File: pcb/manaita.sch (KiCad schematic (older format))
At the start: 105 parts, among them J1 USB_B_Mini, J4 SCK, J6 MOSI, J7 MISO, J8 VCC, J9 GND, SW1 SW_PUSH, SW10 SW_PUSH, SW11 SW_PUSH, SW12 SW_PUSH, SW13 SW_PUSH, SW14 SW_PUSH, SW15 SW_PUSH, SW16 SW_PUSH, SW17 SW_PUSH, SW18 SW_PUSH, SW19 SW_PUSH, SW2 SW_PUSH, SW20 SW_PUSH, SW21 SW_PUSH, SW22 SW_PUSH, SW23 SW_PUSH, SW24 SW_PUSH, SW25 SW_PUSH, SW26 SW_PUSH, SW27 SW_PUSH, SW28 SW_PUSH, SW29 SW_PUSH, SW3 SW_PUSH, SW30 SW_PUSH, SW31 SW_PUSH, SW32 SW_PUSH, SW33 SW_PUSH, SW34 SW_PUSH, SW35 SW_PUSH, SW36 SW_PUSH, SW37 SW_PUSH, SW38 SW_PUSH, SW39 SW_PUSH, SW4 SW_PUSH, SW40 SW_PUSH, SW41 SW_Push, SW5 SW_PUSH, SW6 SW_PUSH, SW7 SW_PUSH, SW8 SW_PUSH, SW9 SW_PUSH, U1 ATmega32U4-AU, Y1 Crystal_GND24_Small

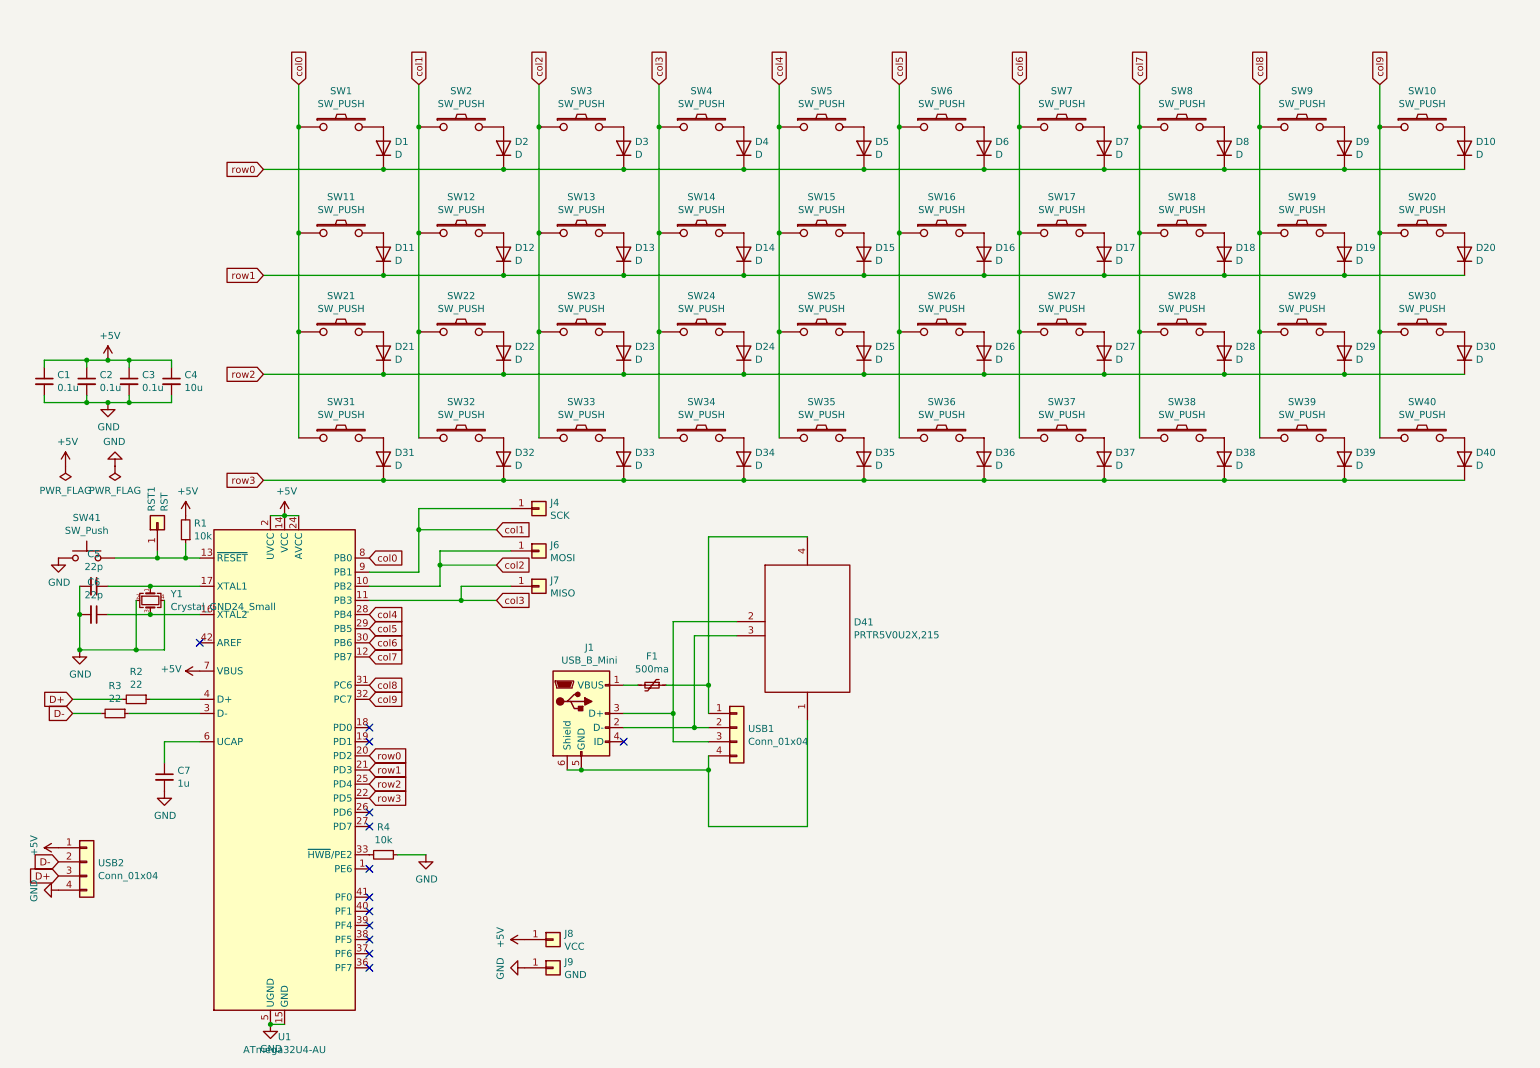
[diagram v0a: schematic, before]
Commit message: :bug: (sch) fix switch
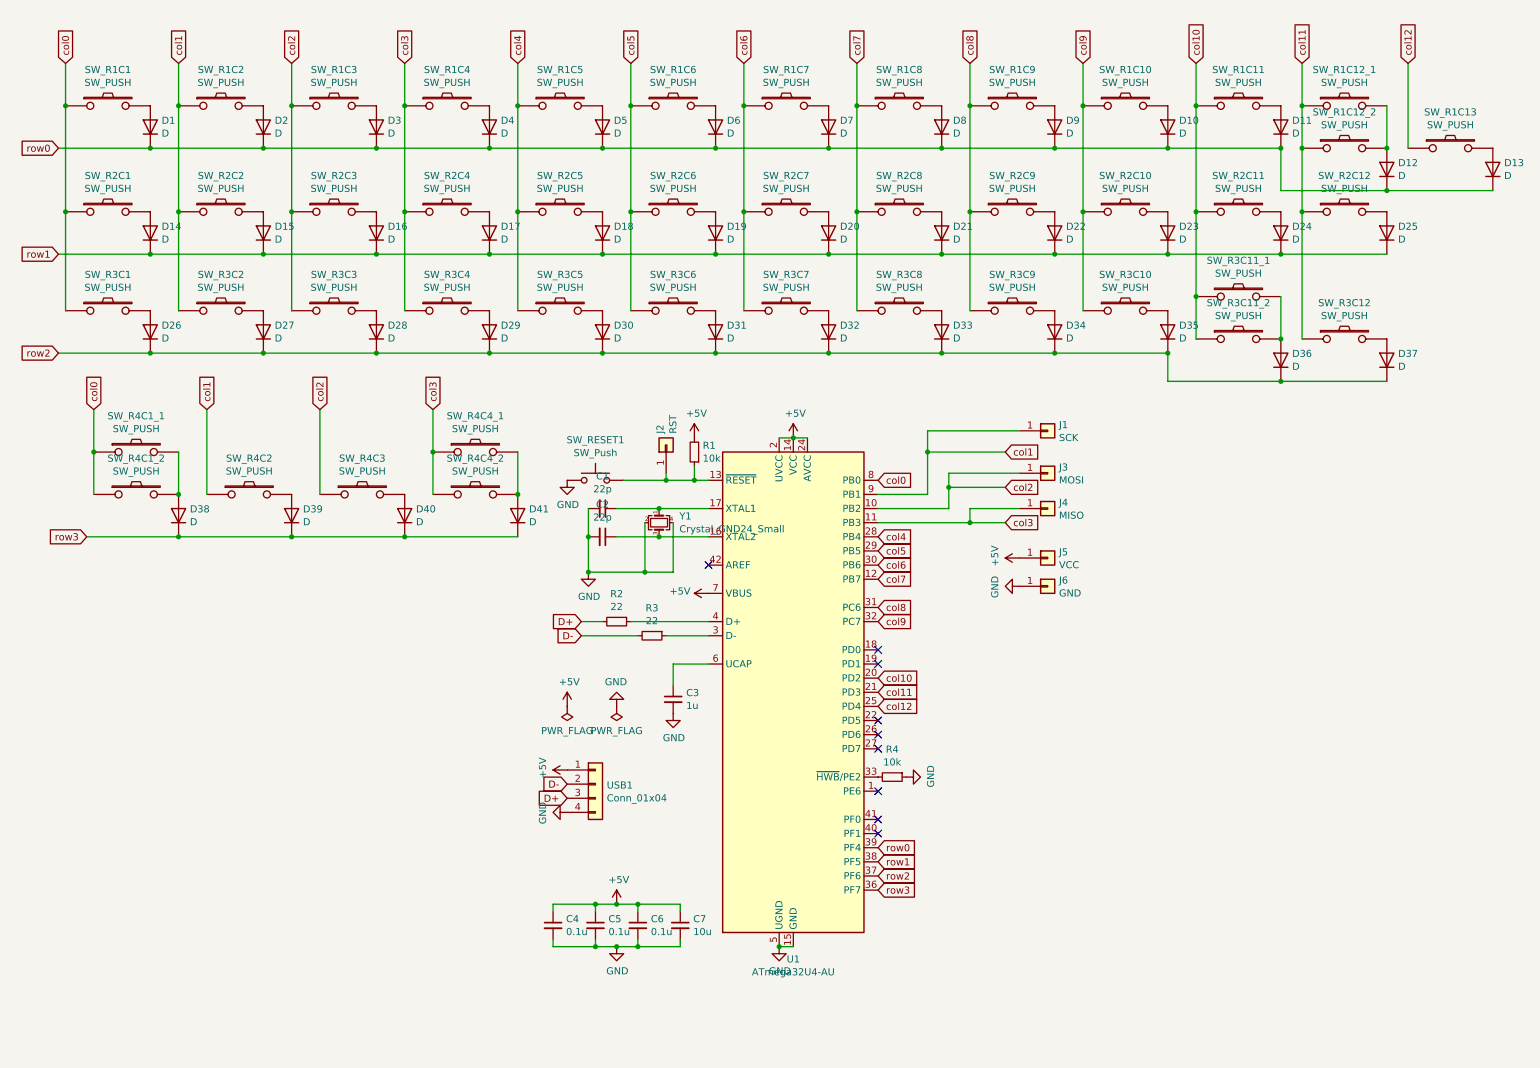
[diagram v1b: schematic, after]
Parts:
- removed D35, D38, D39, D40: D, swanmatch:D3_TH_SMD, symbol Device:D
- removed D41: PRTR5V0U2X,215, digikey:TO-253-4, symbol swanmatch:PRTR5V0U2X,215
- removed F1: 500ma, Fuse:Fuse_1206_3216Metric_Pad1.42x1.75mm_HandSolder, symbol Device:Polyfuse_Small
- removed J1: USB_B_Mini, Connector_USB:USB_Micro-B_Molex-105017-0001, symbol Connector:USB_B_Micro
- removed SW35: SW_PUSH, swanmatch:MX_Hotswap_1u, symbol swanmatch:SW_PUSH
- removed SW36, SW38, SW39: SW_PUSH, swanmatch:MX_Hotswap_1.25u, symbol swanmatch:SW_PUSH
- removed SW37: SW_PUSH, swanmatch:MX_Hotswap_2.25u, symbol swanmatch:SW_PUSH
- removed SW40: SW_PUSH, swanmatch:MX_Hotswap_2.75u, symbol swanmatch:SW_PUSH
- removed USB1: Conn_01x04, Connector_PinHeader_2.54mm:PinHeader_1x04_P2.54mm_Horizontal, symbol Connector_Generic:Conn_01x04
- added D11, D12, D13, D24, D25: D, swanmatch:D3_SMD_v2, symbol Device:D
- added SW_R1C11, SW_R1C12_1, SW_R1C12_2, SW_R1C13, SW_R2C11, SW_R3C11_1: SW_PUSH, mikamo3:CherryMX_Hotswap_1.00u_1side, symbol swanmatch:SW_PUSH
- added SW_R2C12: SW_PUSH, mikamo3:CherryMX_Hotswap_1.75u_1side, symbol swanmatch:SW_PUSH
- added SW_R3C11_2: SW_PUSH, mikamo3:CherryMX_Hotswap_2.25u_1side, symbol swanmatch:SW_PUSH
- added SW_R3C12, SW_R4C1_1, SW_R4C4_1: SW_PUSH, mikamo3:CherryMX_Hotswap_1.25u_1side, symbol swanmatch:SW_PUSH
- D1, D10, D2, D3, D36, D37, D4, D5, D6, D7, D8, D9: footprint swanmatch:D3_TH_SMD -> swanmatch:D3_SMD_v2
- D14: renamed from D11; footprint swanmatch:D3_TH_SMD -> swanmatch:D3_SMD_v2
- D15: renamed from D12; footprint swanmatch:D3_TH_SMD -> swanmatch:D3_SMD_v2
- D16: renamed from D13; footprint swanmatch:D3_TH_SMD -> swanmatch:D3_SMD_v2
- D17: renamed from D14; footprint swanmatch:D3_TH_SMD -> swanmatch:D3_SMD_v2
- D18: renamed from D15; footprint swanmatch:D3_TH_SMD -> swanmatch:D3_SMD_v2
- D19: renamed from D16; footprint swanmatch:D3_TH_SMD -> swanmatch:D3_SMD_v2
- D20: renamed from D17; footprint swanmatch:D3_TH_SMD -> swanmatch:D3_SMD_v2
- D21: renamed from D18; footprint swanmatch:D3_TH_SMD -> swanmatch:D3_SMD_v2
- D22: renamed from D19; footprint swanmatch:D3_TH_SMD -> swanmatch:D3_SMD_v2
- D23: renamed from D20; footprint swanmatch:D3_TH_SMD -> swanmatch:D3_SMD_v2
- D26: renamed from D21; footprint swanmatch:D3_TH_SMD -> swanmatch:D3_SMD_v2
- D27: renamed from D22; footprint swanmatch:D3_TH_SMD -> swanmatch:D3_SMD_v2
- D28: renamed from D23; footprint swanmatch:D3_TH_SMD -> swanmatch:D3_SMD_v2
- D29: renamed from D24; footprint swanmatch:D3_TH_SMD -> swanmatch:D3_SMD_v2
- D30: renamed from D25; footprint swanmatch:D3_TH_SMD -> swanmatch:D3_SMD_v2
- D31: renamed from D26; footprint swanmatch:D3_TH_SMD -> swanmatch:D3_SMD_v2
- D32: renamed from D27; footprint swanmatch:D3_TH_SMD -> swanmatch:D3_SMD_v2
- D33: renamed from D28; footprint swanmatch:D3_TH_SMD -> swanmatch:D3_SMD_v2
- D34: renamed from D29; footprint swanmatch:D3_TH_SMD -> swanmatch:D3_SMD_v2
- D35: renamed from D30; footprint swanmatch:D3_TH_SMD -> swanmatch:D3_SMD_v2
- D38: renamed from D31; footprint swanmatch:D3_TH_SMD -> swanmatch:D3_SMD_v2
- D39: renamed from D32; footprint swanmatch:D3_TH_SMD -> swanmatch:D3_SMD_v2
- D40: renamed from D33; footprint swanmatch:D3_TH_SMD -> swanmatch:D3_SMD_v2
- D41: renamed from D34; footprint swanmatch:D3_TH_SMD -> swanmatch:D3_SMD_v2
- SW_R1C1: renamed from SW1; footprint swanmatch:MX_Hotswap_1u -> mikamo3:CherryMX_Hotswap_1.00u_1side
- SW_R1C10: renamed from SW10; footprint swanmatch:MX_Hotswap_1u -> mikamo3:CherryMX_Hotswap_1.00u_1side
- SW_R1C2: renamed from SW2; footprint swanmatch:MX_Hotswap_1u -> mikamo3:CherryMX_Hotswap_1.00u_1side
- SW_R1C3: renamed from SW3; footprint swanmatch:MX_Hotswap_1u -> mikamo3:CherryMX_Hotswap_1.00u_1side
- SW_R1C4: renamed from SW4; footprint swanmatch:MX_Hotswap_1u -> mikamo3:CherryMX_Hotswap_1.00u_1side
- SW_R1C5: renamed from SW5; footprint swanmatch:MX_Hotswap_1u -> mikamo3:CherryMX_Hotswap_1.00u_1side
- SW_R1C6: renamed from SW6; footprint swanmatch:MX_Hotswap_1u -> mikamo3:CherryMX_Hotswap_1.00u_1side
- SW_R1C7: renamed from SW7; footprint swanmatch:MX_Hotswap_1u -> mikamo3:CherryMX_Hotswap_1.00u_1side
- SW_R1C8: renamed from SW8; footprint swanmatch:MX_Hotswap_1u -> mikamo3:CherryMX_Hotswap_1.00u_1side
- SW_R1C9: renamed from SW9; footprint swanmatch:MX_Hotswap_1u -> mikamo3:CherryMX_Hotswap_1.00u_1side
- SW_R2C1: renamed from SW11; footprint swanmatch:MX_Hotswap_1u -> mikamo3:CherryMX_Hotswap_1.25u_1side
- SW_R2C10: renamed from SW20; footprint swanmatch:MX_Hotswap_1u -> mikamo3:CherryMX_Hotswap_1.00u_1side
- SW_R2C2: renamed from SW12; footprint swanmatch:MX_Hotswap_2u -> mikamo3:CherryMX_Hotswap_1.00u_1side
- SW_R2C3: renamed from SW13; footprint swanmatch:MX_Hotswap_1.25u -> mikamo3:CherryMX_Hotswap_1.00u_1side
- SW_R2C4: renamed from SW14; footprint swanmatch:MX_Hotswap_1u -> mikamo3:CherryMX_Hotswap_1.00u_1side
- SW_R2C5: renamed from SW15; footprint swanmatch:MX_Hotswap_1u -> mikamo3:CherryMX_Hotswap_1.00u_1side
- SW_R2C6: renamed from SW16; footprint swanmatch:MX_Hotswap_1u -> mikamo3:CherryMX_Hotswap_1.00u_1side
- SW_R2C7: renamed from SW17; footprint swanmatch:MX_Hotswap_1u -> mikamo3:CherryMX_Hotswap_1.00u_1side
- SW_R2C8: renamed from SW18; footprint swanmatch:MX_Hotswap_1u -> mikamo3:CherryMX_Hotswap_1.00u_1side
- SW_R2C9: renamed from SW19; footprint swanmatch:MX_Hotswap_1u -> mikamo3:CherryMX_Hotswap_1.00u_1side
- SW_R3C1: renamed from SW21; footprint swanmatch:MX_Hotswap_1u -> mikamo3:CherryMX_Hotswap_1.75u_1side
- SW_R3C10: renamed from SW30; footprint swanmatch:MX_Hotswap_1u -> mikamo3:CherryMX_Hotswap_1.00u_1side
- SW_R3C2: renamed from SW22; footprint swanmatch:MX_Hotswap_1u -> mikamo3:CherryMX_Hotswap_1.00u_1side
- SW_R3C3: renamed from SW23; footprint swanmatch:MX_Hotswap_1u -> mikamo3:CherryMX_Hotswap_1.00u_1side
- SW_R3C4: renamed from SW24; footprint swanmatch:MX_Hotswap_1.75u -> mikamo3:CherryMX_Hotswap_1.00u_1side
- SW_R3C5: renamed from SW25; footprint swanmatch:MX_Hotswap_1.75u -> mikamo3:CherryMX_Hotswap_1.00u_1side
- SW_R3C6: renamed from SW26; footprint swanmatch:MX_Hotswap_1u -> mikamo3:CherryMX_Hotswap_1.00u_1side
- SW_R3C7: renamed from SW27; footprint swanmatch:MX_Hotswap_1u -> mikamo3:CherryMX_Hotswap_1.00u_1side
- SW_R3C8: renamed from SW28; footprint swanmatch:MX_Hotswap_1u -> mikamo3:CherryMX_Hotswap_1.00u_1side
- SW_R3C9: renamed from SW29; footprint swanmatch:MX_Hotswap_1u -> mikamo3:CherryMX_Hotswap_1.00u_1side
- SW_R4C1_2: renamed from SW31; footprint swanmatch:MX_Hotswap_1u -> mikamo3:CherryMX_Hotswap_2.25u_1side
- SW_R4C2: renamed from SW32; footprint swanmatch:MX_Hotswap_1u -> mikamo3:CherryMX_Hotswap_1.25u_1side
- SW_R4C3: renamed from SW33; footprint swanmatch:MX_Hotswap_1u -> mikamo3:CherryMX_Hotswap_1.25u_1side
- SW_R4C4_2: renamed from SW34; footprint swanmatch:MX_Hotswap_1u -> mikamo3:CherryMX_Hotswap_2.75u_1side
- renumbered C5 to C1, C6 to C2, C7 to C3, C1 to C4, C2 to C5, C3 to C6, C4 to C7, J4 to J1, RST1 to J2, J6 to J3, J7 to J4, J8 to J5, J9 to J6, SW41 to SW_RESET1, USB2 to USB1
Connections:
- net col0: now also SW_R4C1_1.1
- net col3: now also SW_R4C4_1.1
- net row0: now also U1.39 (PF4), D11.1 (K), D12.1 (K), D13.1 (K); no longer U1.20 (PD2)
- net row1: now also U1.38 (PF5), D24.1 (K), D25.1 (K); no longer U1.21 (PD3)
- net row2: now also D36.1 (K), D37.1 (K), U1.37 (PF6); no longer U1.25 (PD4)
- net row3: now also U1.36 (PF7); no longer D36.1 (K), D37.1 (K), U1.22 (PD5)
- net at D41.2 (A), SW_R4C4_2.2: now also SW_R4C4_1.2
- net at D36.2 (A): now also SW_R3C11_1.2, SW_R3C11_2.2
- net at D37.2 (A): now also SW_R3C12.2
- net at D38.2 (A), SW_R4C1_2.2: now also SW_R4C1_1.2
- new net: D11.2 (A), SW_R1C11.2
- new net: D12.2 (A), SW_R1C12_1.2, SW_R1C12_2.2
- new net: D13.2 (A), SW_R1C13.2
- new net: D24.2 (A), SW_R2C11.2
- new net: D25.2 (A), SW_R2C12.2
- new net col10: SW_R1C11.1, SW_R2C11.1, SW_R3C11_1.1, SW_R3C11_2.1, U1.20 (PD2)
- new net col11: SW_R1C12_1.1, SW_R1C12_2.1, SW_R2C12.1, SW_R3C12.1, U1.21 (PD3)
- new net col12: SW_R1C13.1, U1.25 (PD4)
- no-connect marks 13 -> 9
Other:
- moved on the sheet: C1, C2, C3, C4, C5, C6, C7, D1, D10, D14, D15, D16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

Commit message: :sparkles: (pcb) add pcb
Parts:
- SW_R1C12_2: footprint mikamo3:CherryMX_Hotswap_1.00u_1side -> mikamo3:CherryMX_Hotswap_1.75u_1side
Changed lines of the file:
@@
 F 0 "SW_R1C12_2" H 9850 1605 50  0000 C CNN
 F 1 "SW_PUSH" H 9850 1514 50  0000 C CNN
-F 2 "mikamo3:CherryMX_Hotswap_1.00u_1side" H 9850 1350 50  0001 C CNN
+F 2 "mikamo3:CherryMX_Hotswap_1.75u_1side" H 9850 1350 50  0001 C CNN
 F 3 "" H 9850 1350 50  0000 C CNN
 	1    9850 1350

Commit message: WIP
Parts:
- USB1: footprint Connector_PinHeader_2.54mm:PinHeader_1x04_P2.54mm_Horizontal -> Connector_JST:JST_EH_S4B-EH_1x04_P2.50mm_Horizontal
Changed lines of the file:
@@
 F 0 "USB1" H 4630 5842 50  0000 L CNN
 F 1 "Conn_01x04" H 4630 5751 50  0000 L CNN
-F 2 "Connector_PinHeader_2.54mm:PinHeader_1x04_P2.54mm_Horizontal" H 4550 5850 50  0001 C CNN
+F 2 "Connector_JST:JST_EH_S4B-EH_1x04_P2.50mm_Horizontal" H 4550 5850 50  0001 C CNN
 F 3 "~" H 4550 5850 50  0001 C CNN
 	1    4550 5850

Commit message: :construction: (all) WIP
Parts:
- added D42, D43: D_Zener, Diode_SMD:D_SOD-123, symbol Device:D_Zener
- added F1: 500mA, Fuse:Fuse_0805_2012Metric_Pad1.15x1.40mm_HandSolder, symbol Device:Polyfuse_Small
- USB1: footprint Connector_JST:JST_EH_S4B-EH_1x04_P2.50mm_Horizontal -> Connector_PinHeader_2.54mm:PinHeader_1x04_P2.54mm_Horizontal
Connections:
- net +5V: now also F1.2; no longer USB1.1 (Pin_1)
- net D+: now also D42.1 (K)
- net D-: now also D43.1 (K)
- net GND: now also D42.2 (A), D43.2 (A)
- net col0: now also U1.36 (PF7); no longer U1.8 (PB0)
- net col1: now also U1.25 (PD4); no longer U1.9 (PB1)
- net col10: now also U1.9 (PB1); no longer U1.20 (PD2)
- net col11: now also U1.10 (PB2); no longer U1.21 (PD3)
- net col12: now also U1.11 (PB3); no longer U1.25 (PD4)
- net col2: now also U1.26 (PD6); no longer U1.10 (PB2)
- net col3: now also U1.27 (PD7); no longer U1.11 (PB3)
- net col4: now also U1.37 (PF6); no longer U1.28 (PB4)
- net col5: now also U1.38 (PF5); no longer U1.29 (PB5)
- net col6: now also U1.39 (PF4); no longer U1.30 (PB6)
- net col7: now also U1.28 (PB4); no longer U1.12 (PB7)
- net col8: now also U1.29 (PB5); no longer U1.31 (PC6)
- net col9: now also U1.12 (PB7); no longer U1.32 (PC7)
- net row0: now also U1.32 (PC7); no longer U1.39 (PF4)
- net row1: now also U1.31 (PC6); no longer U1.38 (PF5)
- net row2: now also U1.30 (PB6); no longer U1.37 (PF6)
- net row3: now also U1.8 (PB0); no longer U1.36 (PF7)
- new net: F1.1, USB1.1 (Pin_1)
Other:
- moved on the sheet: C4, C5, C6, C7, J1, J3, J4, J5, J6, USB1

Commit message: create pcb done
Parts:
- D1, D10, D11, D12, D13, D14, D15, D16, D17, D18, D19, D2, D20, D21, D22, D23, D24, D25, D26, D27, D28, D29, D3, D30, D31, D32, D33, D34, D35, D36, D37, D38, D39, D4, D40, D41, D5, D6, D7, D8, D9: footprint swanmatch:D3_SMD_v2 -> mikamo3:D3_SMD_1side
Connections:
- net col0: now also U1.1 (PE6); no longer U1.36 (PF7)
- net col1: now also U1.41 (PF0); no longer U1.25 (PD4)
- net col10: now also U1.29 (PB5); no longer U1.9 (PB1)
- net col11: now also U1.28 (PB4); no longer U1.10 (PB2)
- net col12: now also U1.25 (PD4); no longer U1.11 (PB3)
- net col2: now also U1.40 (PF1); no longer U1.26 (PD6)
- net col3: now also U1.39 (PF4); no longer U1.27 (PD7)
- net col4: now also U1.38 (PF5); no longer U1.37 (PF6)
- net col5: now also U1.37 (PF6); no longer U1.38 (PF5)
- net col6: now also U1.36 (PF7); no longer U1.39 (PF4)
- net col7: now also U1.32 (PC7); no longer U1.28 (PB4)
- net col8: now also U1.31 (PC6); no longer U1.29 (PB5)
- net col9: now also U1.30 (PB6); no longer U1.12 (PB7)
- net row0: now also U1.11 (PB3); no longer U1.32 (PC7)
- net row1: now also U1.10 (PB2); no longer U1.31 (PC6)
- net row2: now also U1.9 (PB1); no longer U1.30 (PB6)
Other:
- moved on the sheet: C1, C2, C3, D42, D43, J1, J2, J3, J4, J5, J6, R1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

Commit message: :sparkles: (pcb) fix chore
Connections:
- net col0: now also J4.1 (Pin_1), U1.11 (PB3); no longer U1.1 (PE6)
- net col1: now also J3.1 (Pin_1), U1.10 (PB2); no longer J1.1 (Pin_1), U1.41 (PF0)
- net col2: now also J1.1 (Pin_1), U1.9 (PB1); no longer J3.1 (Pin_1), U1.40 (PF1)
- net col3: now also U1.8 (PB0); no longer J4.1 (Pin_1), U1.39 (PF4)
- net row0: now also U1.1 (PE6); no longer U1.11 (PB3)
- net row1: now also U1.41 (PF0); no longer U1.10 (PB2)
- net row2: now also U1.40 (PF1); no longer U1.9 (PB1)
- net row3: now also U1.39 (PF4); no longer U1.8 (PB0)
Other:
- moved on the sheet: J1, J3, J4
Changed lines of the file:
@@
 	4800 3600 4800 3800
 Connection ~ 4800 3800
-Text GLabel 6850 3700 2    50   Input ~ 0
+Text GLabel 6850 5600 2    50   Input ~ 0
 row0
-Text GLabel 6850 3500 2    50   Input ~ 0
+Text GLabel 6850 5900 2    50   Input ~ 0
 row2
-Text GLabel 6850 3600 2    50   Input ~ 0
+Text GLabel 6850 5800 2    50   Input ~ 0
 row1
+Text GLabel 6850 6000 2    50   Input ~ 0
+row3
+Text GLabel 7850 3850 2    50   Input ~ 0
+col0
+Text GLabel 7850 3600 2    50   Input ~ 0
+col1
+Text GLabel 7400 3500 2    50   Input ~ 0
+col2
 Text GLabel 6850 3400 2    50   Input ~ 0
-row3
-Text GLabel 6850 5600 2    50   Input ~ 0
-col0
-Text GLabel 8350 5800 2    50   Input ~ 0
-col1
-Text GLabel 8350 6000 2    50   Input ~ 0
-col2
-Text GLabel 8350 6250 2    50   Input ~ 0
 col3
 Text GLabel 6850 6100 2    50   Input ~ 0
@@
 L Connector_Generic:Conn_01x01 J4
 U 1 1 5FB79428
-P 8650 6150
-F 0 "J4" H 8730 6192 50  0000 L CNN
-F 1 "MISO" H 8730 6101 50  0000 L CNN
-F 2 "swanmatch:1pin_conn" H 8650 6150 50  0001 C CNN
-F 3 "~" H 8650 6150 50  0001 C CNN
-	1    8650 6150
+P 8150 3700
+F 0 "J4" H 8230 3742 50  0000 L CNN
+F 1 "MISO" H 8230 3651 50  0000 L CNN
+F 2 "swanmatch:1pin_conn" H 8150 3700 50  0001 C CNN
+F 3 "~" H 8150 3700 50  0001 C CNN
+	1    8150 3700
 	1    0    0    -1
 $EndComp
@@
 L Connector_Generic:Conn_01x01 J3
 U 1 1 5FB79976
-P 8650 5900
-F 0 "J3" H 8730 5942 50  0000 L CNN
-F 1 "MOSI" H 8730 5851 50  0000 L CNN
-F 2 "swanmatch:1pin_conn" H 8650 5900 50  0001 C CNN
-F 3 "~" H 8650 5900 50  0001 C CNN
-	1    8650 5900
+P 8050 3450
+F 0 "J3" H 8130 3492 50  0000 L CNN
+F 1 "MOSI" H 8130 3401 50  0000 L CNN
+F 2 "swanmatch:1pin_conn" H 8050 3450 50  0001 C CNN
+F 3 "~" H 8050 3450 50  0001 C CNN
+	1    8050 3450
 	1    0    0    -1
 $EndComp
@@
 L Connector_Generic:Conn_01x01 J1
 U 1 1 5FB79F9C
-P 8650 5650
-F 0 "J1" H 8730 5692 50  0000 L CNN
-F 1 "SCK" H 8730 5601 50  0000 L CNN
-F 2 "swanmatch:1pin_conn" H 8650 5650 50  0001 C CNN
-F 3 "~" H 8650 5650 50  0001 C CNN
-	1    8650 5650
+P 7550 3350
+F 0 "J1" H 7630 3392 50  0000 L CNN
+F 1 "SCK" H 7630 3301 50  0000 L CNN
+F 2 "swanmatch:1pin_conn" H 7550 3350 50  0001 C CNN
+F 3 "~" H 7550 3350 50  0001 C CNN
+	1    7550 3350
 	1    0    0    -1
 $EndComp
@@
 	0    -1   -1   0
 $EndComp
-Wire Wire Line
-	7600 6000 7950 6000
-Wire Wire Line
-	7950 6000 8350 6000
-Wire Wire Line
-	8450 5900 7950 5900
-Wire Wire Line
-	6850 5800 7950 5800
-Wire Wire Line
-	7950 5800 8350 5800
-Wire Wire Line
-	8450 5650 7950 5650
-Wire Wire Line
-	7950 5650 7950 5800
-Connection ~ 7950 5800
 $Comp
 L power:GND #PWR06
@@
 Wire Wire Line
 	4500 4400 4900 4400
-Connection ~ 7950 6000
-Wire Wire Line
-	7950 5900 7950 6000
-Wire Wire Line
-	8350 6250 7950 6250
-Wire Wire Line
-	7950 6250 7950 6150
-Connection ~ 7950 6150
-Wire Wire Line
-	7950 6150 8450 6150
 Wire Wire Line
 	6850 5500 7150 5500
 Text GLabel 4150 4500 0    50   Input ~ 0
 D-
-Wire Wire Line
-	6850 5900 7600 5900
-Wire Wire Line
-	7600 5900 7600 6000
-Wire Wire Line
-	6850 6000 7500 6000
-Wire Wire Line
-	7500 6000 7500 6150
-Wire Wire Line
-	7500 6150 7950 6150
 $Comp
 L MCU_Microchip_ATmega:ATmega32U4-AU U1
@@
 NoConn ~ 6850 5300
 NoConn ~ 6850 4100
+Wire Wire Line
+	6850 3500 7350 3500
+Wire Wire Line
+	7350 3500 7350 3350
+Wire Wire Line
+	7350 3500 7400 3500
+Connection ~ 7350 3500
+Wire Wire Line
+	6850 3600 7700 3600
+Wire Wire Line
+	7850 3450 7700 3450
+Wire Wire Line
+	7700 3450 7700 3600
+Connection ~ 7700 3600
+Wire Wire Line
+	7700 3600 7850 3600
+Wire Wire Line
+	6850 3700 7700 3700
+Wire Wire Line
+	7700 3700 7700 3850
+Wire Wire Line
+	7700 3850 7850 3850
+Connection ~ 7700 3700
+Wire Wire Line
+	7700 3700 7950 3700
 $EndSCHEMATC
